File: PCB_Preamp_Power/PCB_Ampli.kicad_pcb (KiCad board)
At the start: 4 copper layers, 146.6 x 110.8 mm, 85 parts, among them J1 Conn_01x02, J2 Jack-DC, J3 Conn_01x02, J4 Conn_01x02, SW1 SW_Push_DPDT, SW2 SW_Push_DPDT, SW3 SW_SPDT, SW4 SW_SPDT

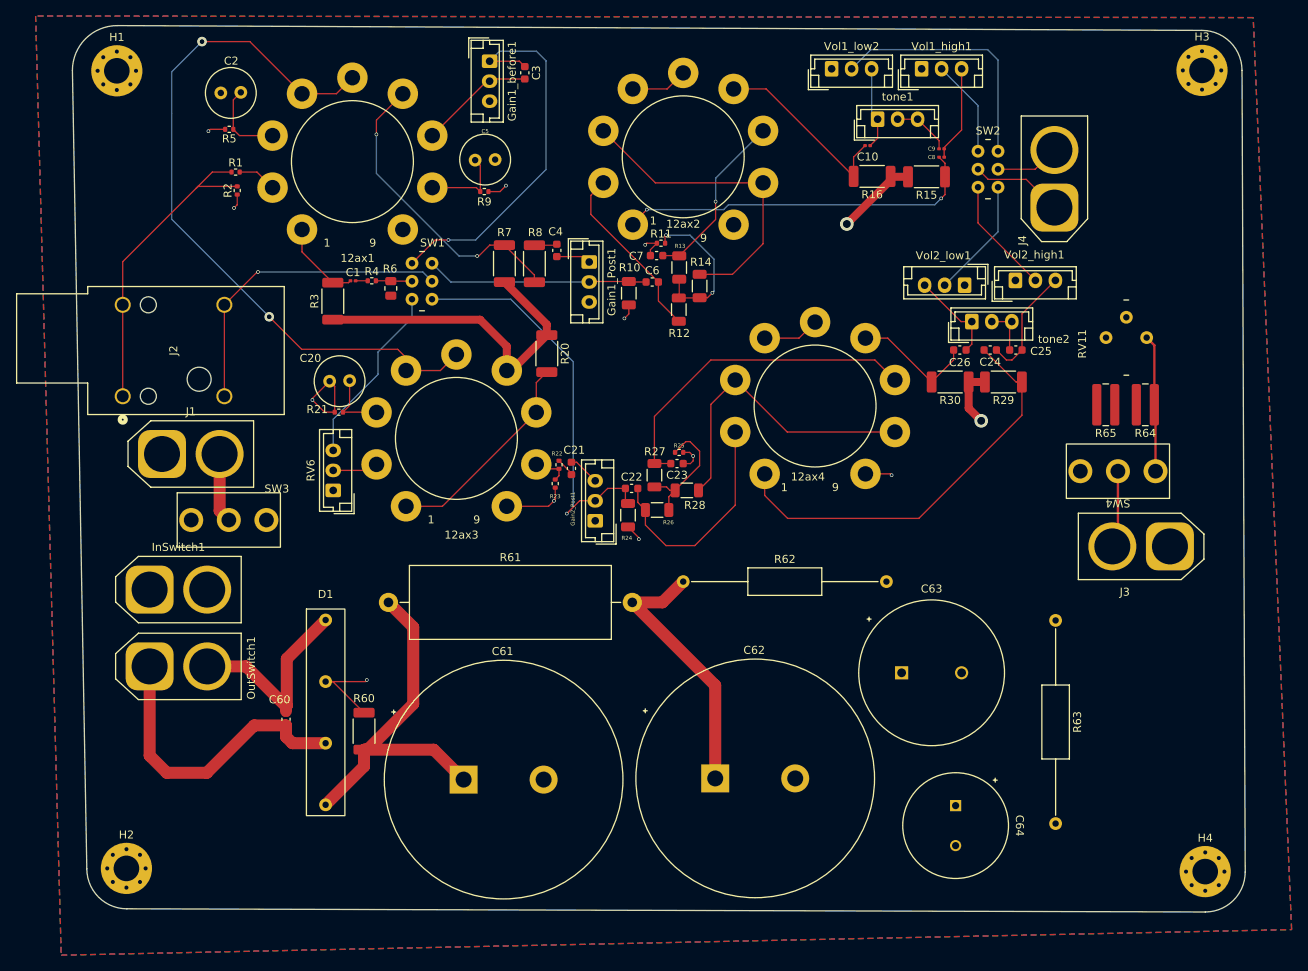
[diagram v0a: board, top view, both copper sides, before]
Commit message: PCBV4_Connectors_changed
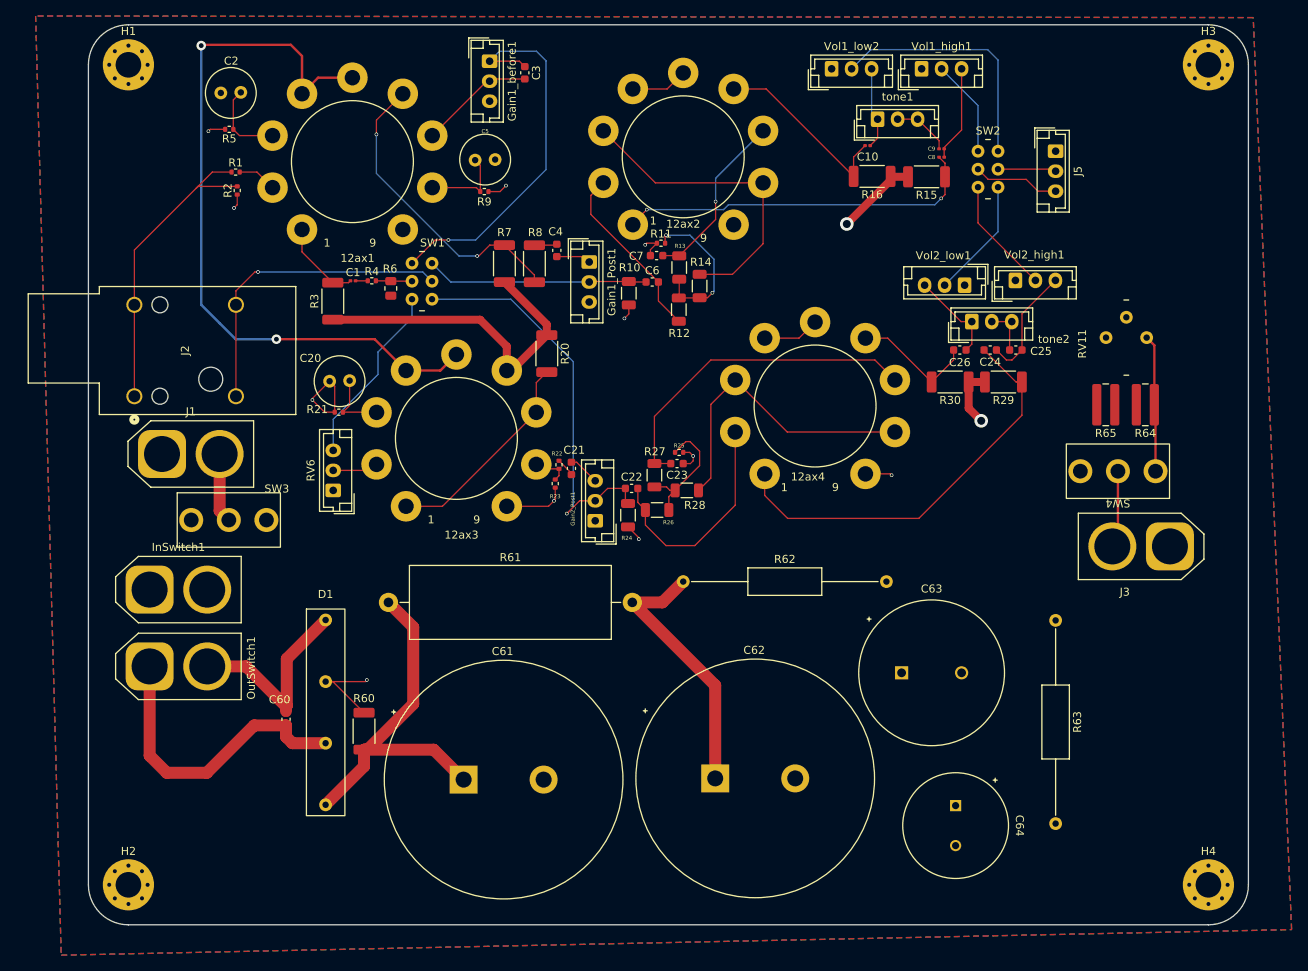
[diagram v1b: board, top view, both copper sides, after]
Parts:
- removed J4: Conn_01x02, Connector_AMASS:AMASS_XT60-M_1x02_P7.20mm_Vertical
- added J5: Conn_01x03, Connector_JST:JST_EH_B3B-EH-A_1x03_P2.50mm_Vertical, F.Cu at (145.9, 48.3)
- moved H2 2.07 mm to (30.0, 140.0)
- moved H4 1.70 mm to (165.0, 140.0)
- moved H1 1.63 mm to (30.0, 37.5)
- moved J2 1.45 mm to (30.7, 78.9)
- moved H3 1.06 mm to (165.0, 37.5)
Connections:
- InSwitch1 pad 1: Heater1_B -> +250V
- InSwitch1 pad 2: +250V -> Heater1_B
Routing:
- net Heater1_A: track 122.7 -> 126.2 mm
- net Net-(J5-Pin_2): track 8.04 -> 7.30 mm
- net Net-(J5-Pin_3): track 11.5 -> 10.8 mm
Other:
- board size 146.6 x 110.8 mm -> 145 x 112.5 mm
